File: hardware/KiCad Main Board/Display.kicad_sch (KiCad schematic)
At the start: 22 parts, among them J3 Display_Connector-0.5mmZIF-AE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, J5 RAKA, Q1 AO3400A

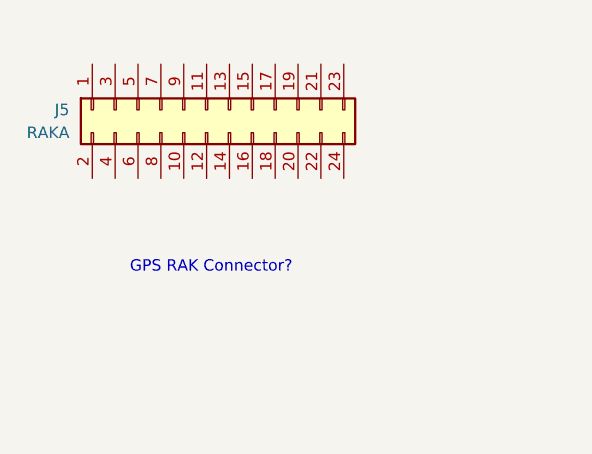
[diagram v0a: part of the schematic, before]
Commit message: added connector for RF daughter board
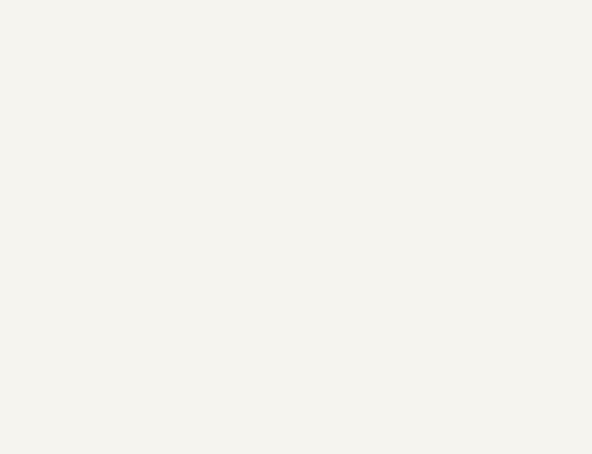
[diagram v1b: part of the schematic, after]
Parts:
- removed J5: RAKA, symbol Connector_Generic:Conn_02x12_Odd_Even
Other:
- note removed: "GPS RAK Connector?"
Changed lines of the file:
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@@
 	(generator_version "9.0")
 	(paper "A4")
-	(text "GPS RAK Connector?\n"
-		(exclude_from_sim no)
-		(at 75.438 64.516 0)
-		(effects
-			(font
-				(size 1.27 1.27)
-			)
-		)
-	)
 	(text "Display\n"
 		(exclude_from_sim no)
@@
 					(unit 1)
 				)
-			)
-		)
-	)
-	(symbol
-		(lib_id "Connector_Generic:Conn_02x12_Odd_Even")
-		(at 74.93 46.99 90)
-		(mirror x)
-		(unit 1)
-		(exclude_from_sim no)
-		(in_bom yes)
-		(on_board yes)
-		(dnp no)
-		(fields_autoplaced yes)
-		(property "Reference" "J5"
-			(at 59.69 46.9899 90)
-			(effects
-				(font
-					(size 1.27 1.27)
-				)
-				(justify left)
-			)
-		)
-		(property "Value" "RAKA"
-			(at 59.69 49.5299 90)
-			(effects
-				(font
-					(size 1.27 1.27)
-				)
-				(justify left)
-			)
-		)
-		(property "Footprint" ""
-			(at 74.93 46.99 0)
-			(effects
-				(font
-					(size 1.27 1.27)
-				)
-				(hide yes)
-			)
-		)
-		(property "Datasheet" "~"
-			(at 74.93 46.99 0)
-			(effects
-				(font
-					(size 1.27 1.27)
-				)
-				(hide yes)
-			)
-		)
-		(property "Description" "Generic connector, double row, 02x12, odd/even pin numbering scheme (row 1 odd numbers, row 2 even numbers), script generated (kicad-library-utils/schlib/autogen/connector/)"
-			(at 74.93 46.99 0)
-			(effects
-				(font
-					(size 1.27 1.27)
-				)
-				(hide yes)
-			)
-		)
-		(pin "19"
-		)
-		(pin "11"
-		)
-		(pin "7"
-		)
-		(pin "23"
-		)
-		(pin "12"
-		)
-		(pin "16"
-		)
-		(pin "5"
-		)
-		(pin "21"
-		)
-		(pin "6"
-		)
-		(pin "2"
-		)
-		(pin "15"
-		)
-		(pin "9"
-		)
-		(pin "1"
-		)
-		(pin "3"
-		)
-		(pin "13"
-		)
-		(pin "17"
-		)
-		(pin "4"
-		)
-		(pin "8"
-		)
-		(pin "10"
-		)
-		(pin "14"
-		)
-		(pin "18"
-		)
-		(pin "20"
-		)
-		(pin "22"
-		)
-		(pin "24"
-		)
-		(instances
-			(project ""
-				(path "/fd5c68a7-f5d0-4135-a258-bde3ebf63307/b6409364-80a7-45e6-8438-6c9767ff2100"
-					(reference "J5")
-					(unit 1)
-				)

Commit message: working on PCB
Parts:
- removed D1, D2, D3: MBR0530, Diode_SMD:D_SOD-123, symbol Diode:MBR0530
- added D56, D57, D58: B340, Diode_SMD:D_SMC, symbol Diode:B340
- J3: value Display_Connector-0.5mmZIF-AES200200A00-1.54ENRS -> FH12-24S-0.5SH(55); footprint (none) -> Connector_FFC-FPC:Hirose_FH12-24S-0.5SH_1x24-1MP_P0.50mm_Horizontal
- L2: footprint (none) -> Inductor_SMD:L_10.4x10.4_H4.8
- R13: footprint (none) -> Resistor_SMD:R_0805_2012Metric_Pad1.20x1.40mm_HandSolder
- R14, R15, R16: footprint (none) -> Resistor_SMD:R_0603_1608Metric_Pad0.98x0.95mm_HandSolder
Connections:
- net GND: now also D57.1 (K)
- net at C28.2, J3.21 (Pin_21): now also D58.1 (K)
- net at C26.1: now also D56.1 (K), D57.2 (A)
- net at C27.2, J3.23 (Pin_23): now also D56.2 (A)
- net at C26.2, L2.1, Q1.3 (D): now also D58.2 (A)
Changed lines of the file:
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@@
 			)
 		)
-		(property "Footprint" ""
+		(property "Footprint" "Resistor_SMD:R_0603_1608Metric_Pad0.98x0.95mm_HandSolder"
 			(at 204.47 114.3 0)
 			(effects
@@
 	)
 	(symbol
+		(lib_id "Diode:B340")
+		(at 195.58 59.69 0)
+		(unit 1)
+		(exclude_from_sim no)
+		(in_bom yes)
+		(on_board yes)
+		(dnp no)
+		(fields_autoplaced yes)
+		(property "Reference" "D58"
+			(at 195.2625 53.34 0)
+			(effects
+				(font
+					(size 1.27 1.27)
+				)
+			)
+		)
+		(property "Value" "B340"
+			(at 195.2625 55.88 0)
+			(effects
+				(font
+					(size 1.27 1.27)
+				)
+			)
+		)
+		(property "Footprint" "Diode_SMD:D_SMC"
+			(at 195.58 64.135 0)
+			(effects
+				(font
+					(size 1.27 1.27)
+				)
+				(hide yes)
+			)
+		)
+		(property "Datasheet" "http://www.jameco.com/Jameco/Products/ProdDS/1538777.pdf"
+			(at 195.58 59.69 0)
+			(effects
+				(font
+					(size 1.27 1.27)
+				)
+				(hide yes)
+			)
+		)
+		(property "Description" "40V 3A Schottky Barrier Rectifier Diode, SMC"
+			(at 195.58 59.69 0)
+			(effects
+				(font
+					(size 1.27 1.27)
+				)
+				(hide yes)
+			)
+		)
+		(pin "1"
+		)
+		(pin "2"
+		)
+		(instances
+			(project "OSS Radio Hardware Design"
+				(path "/fd5c68a7-f5d0-4135-a258-bde3ebf63307/b6409364-80a7-45e6-8438-6c9767ff2100"
+					(reference "D58")
+					(unit 1)
+				)
+			)
+		)
+	)
+	(symbol
 		(lib_id "Device:R_Small")
 		(at 212.09 99.06 270)
@@
 			)
 		)
-		(property "Footprint" ""
+		(property "Footprint" "Resistor_SMD:R_0603_1608Metric_Pad0.98x0.95mm_HandSolder"
 			(at 212.09 99.06 0)
 			(effects
@@
 	)
 	(symbol
-		(lib_id "Diode:MBR0530")
-		(at 213.36 46.99 180)
-		(unit 1)
-		(exclude_from_sim no)
-		(in_bom yes)
-		(on_board yes)
-		(dnp no)
-		(fields_autoplaced yes)
-		(property "Reference" "D3"
-			(at 213.6775 40.64 0)
-			(effects
-				(font
-					(size 1.27 1.27)
-				)
-			)
-		)
-		(property "Value" "MBR0530"
-			(at 213.6775 43.18 0)
-			(effects
-				(font
-					(size 1.27 1.27)
-				)
-			)
-		)
-		(property "Footprint" "Diode_SMD:D_SOD-123"
-			(at 213.36 42.545 0)
-			(effects
-				(font
-					(size 1.27 1.27)
-				)
-				(hide yes)
-			)
-		)
-		(property "Datasheet" "http://www.mccsemi.com/up_pdf/MBR0520~MBR0580(SOD123).pdf"
-			(at 213.36 46.99 0)
-			(effects
-				(font
-					(size 1.27 1.27)
-				)
-				(hide yes)
-			)
-		)
-		(property "Description" "30V 0.5A Schottky Power Rectifier Diode, SOD-123"
-			(at 213.36 46.99 0)
-			(effects
-				(font
-					(size 1.27 1.27)
-				)
-				(hide yes)
-			)
-		)
-		(pin "1"
-		)
-		(pin "2"
-		)
-		(instances
-			(project "OSS Radio Hardware Design"
-				(path "/fd5c68a7-f5d0-4135-a258-bde3ebf63307/b6409364-80a7-45e6-8438-6c9767ff2100"
-					(reference "D3")
-					(unit 1)
-				)
-			)
-		)
-	)
-	(symbol
 		(lib_id "power:GND")
 		(at 166.37 38.1 270)
@@
 			)
 		)
-		(property "Footprint" ""
+		(property "Footprint" "Resistor_SMD:R_0603_1608Metric_Pad0.98x0.95mm_HandSolder"
 			(at 214.63 91.44 0)
 			(effects
@@
 	)
 	(symbol
+		(lib_id "Diode:B340")
+		(at 213.36 46.99 180)
+		(unit 1)
+		(exclude_from_sim no)
+		(in_bom yes)
+		(on_board yes)
+		(dnp no)
+		(fields_autoplaced yes)
+		(property "Reference" "D57"
+			(at 213.6775 40.64 0)
+			(effects
+				(font
+					(size 1.27 1.27)
+				)
+			)
+		)
+		(property "Value" "B340"
+			(at 213.6775 43.18 0)
+			(effects
+				(font
+					(size 1.27 1.27)
+				)
+			)
+		)
+		(property "Footprint" "Diode_SMD:D_SMC"
+			(at 213.36 42.545 0)
+			(effects
+				(font
+					(size 1.27 1.27)
+				)
+				(hide yes)
+			)
+		)
+		(property "Datasheet" "http://www.jameco.com/Jameco/Products/ProdDS/1538777.pdf"
+			(at 213.36 46.99 0)
+			(effects
+				(font
+					(size 1.27 1.27)
+				)
+				(hide yes)
+			)
+		)
+		(property "Description" "40V 3A Schottky Barrier Rectifier Diode, SMC"
+			(at 213.36 46.99 0)
+			(effects
+				(font
+					(size 1.27 1.27)
+				)
+				(hide yes)
+			)
+		)
+		(pin "1"
+		)
+		(pin "2"
+		)
+		(instances
+			(project "OSS Radio Hardware Design"
+				(path "/fd5c68a7-f5d0-4135-a258-bde3ebf63307/b6409364-80a7-45e6-8438-6c9767ff2100"
+					(reference "D57")
+					(unit 1)
+				)
+			)
+		)
+	)
+	(symbol
 		(lib_id "Device:R_Small")
 		(at 196.85 78.74 90)
@@
 			)
 		)
-		(property "Footprint" ""
+		(property "Footprint" "Resistor_SMD:R_0805_2012Metric_Pad1.20x1.40mm_HandSolder"
 			(at 196.85 78.74 0)
 			(effects
@@
 	)
 	(symbol
+		(lib_id "Diode:B340")
+		(at 195.58 46.99 180)
+		(unit 1)
+		(exclude_from_sim no)
+		(in_bom yes)
+		(on_board yes)
+		(dnp no)
+		(fields_autoplaced yes)
+		(property "Reference" "D56"
+			(at 195.8975 40.64 0)
+			(effects
+				(font
+					(size 1.27 1.27)
+				)
+			)
+		)
+		(property "Value" "B340"
+			(at 195.8975 43.18 0)
+			(effects
+				(font
+					(size 1.27 1.27)
+				)
+			)
+		)
+		(property "Footprint" "Diode_SMD:D_SMC"
+			(at 195.58 42.545 0)
+			(effects
+				(font
+					(size 1.27 1.27)
+				)
+				(hide yes)
+			)
+		)
+		(property "Datasheet" "http://www.jameco.com/Jameco/Products/ProdDS/1538777.pdf"
+			(at 195.58 46.99 0)
+			(effects
+				(font
+					(size 1.27 1.27)
+				)
+				(hide yes)
+			)
+		)
+		(property "Description" "40V 3A Schottky Barrier Rectifier Diode, SMC"
+			(at 195.58 46.99 0)
+			(effects
+				(font
+					(size 1.27 1.27)
+				)
+				(hide yes)
+			)
+		)
+		(pin "1"
+		)
+		(pin "2"
+		)
+		(instances
+			(project "OSS Radio Hardware Design"
+				(path "/fd5c68a7-f5d0-4135-a258-bde3ebf63307/b6409364-80a7-45e6-8438-6c9767ff2100"
+					(reference "D56")
+					(unit 1)
+				)
+			)
+		)
+	)
+	(symbol
 		(lib_id "Device:C_Small")
 		(at 223.52 83.82 90)
@@
 			)
 		)
-		(property "Footprint" ""
+		(property "Footprint" "Inductor_SMD:L_10.4x10.4_H4.8"
 			(at 219.71 59.69 0)
 			(effects
@@
 			)
 		)
-		(property "Datasheet" "~"
+		(property "Datasheet" "SMDRH104R-470MT"
 			(at 219.71 59.69 0)
 			(effects
@@
 			)
 		)
-		(property "Value" "Display_Connector-0.5mmZIF-AES200200A00-1.54ENRS"
+		(property "Value" "FH12-24S-0.5SH(55)"
 			(at 244.348 77.47 90)
 			(effects
@@
 			)
 		)
-		(property "Footprint" ""
+		(property "Footprint" "Connector_FFC-FPC:Hirose_FH12-24S-0.5SH_1x24-1MP_P0.50mm_Horizontal"
 			(at 238.76 101.6 0)
 			(effects
@@
 				(path "/fd5c68a7-f5d0-4135-a258-bde3ebf63307/b6409364-80a7-45e6-8438-6c9767ff2100"
 					(reference "J3")
-					(unit 1)
-				)
-			)
-		)
-	)
-	(symbol
-		(lib_id "Diode:MBR0530")
-		(at 195.58 46.99 180)
-		(unit 1)
-		(exclude_from_sim no)
-		(in_bom yes)
-		(on_board yes)
-		(dnp no)
-		(fields_autoplaced yes)
-		(property "Reference" "D2"
-			(at 195.8975 40.64 0)
-			(effects
-				(font
-					(size 1.27 1.27)
-				)
-			)
-		)
-		(property "Value" "MBR0530"
-			(at 195.8975 43.18 0)
-			(effects
-				(font
-					(size 1.27 1.27)
-				)
-			)
-		)
-		(property "Footprint" "Diode_SMD:D_SOD-123"
-			(at 195.58 42.545 0)
-			(effects
-				(font
-					(size 1.27 1.27)
-				)
-				(hide yes)
-			)
-		)
-		(property "Datasheet" "http://www.mccsemi.com/up_pdf/MBR0520~MBR0580(SOD123).pdf"
-			(at 195.58 46.99 0)
-			(effects
-				(font
-					(size 1.27 1.27)
-				)
-				(hide yes)
-			)
-		)
-		(property "Description" "30V 0.5A Schottky Power Rectifier Diode, SOD-123"
-			(at 195.58 46.99 0)
-			(effects
-				(font
-					(size 1.27 1.27)
-				)
-				(hide yes)
-			)
-		)
-		(pin "1"
-		)
-		(pin "2"
-		)
-		(instances
-			(project "OSS Radio Hardware Design"
-				(path "/fd5c68a7-f5d0-4135-a258-bde3ebf63307/b6409364-80a7-45e6-8438-6c9767ff2100"
-					(reference "D2")
 					(unit 1)
 				)
@@
 					(unit 1)
 				)
-			)
-		)
-	)
-	(symbol
-		(lib_id "Diode:MBR0530")
-		(at 195.58 59.69 0)
-		(unit 1)
-		(exclude_from_sim no)
-		(in_bom yes)
-		(on_board yes)
-		(dnp no)
-		(fields_autoplaced yes)
-		(property "Reference" "D1"
-			(at 195.2625 53.34 0)
-			(effects
-				(font
-					(size 1.27 1.27)
-				)
-			)
-		)
-		(property "Value" "MBR0530"
-			(at 195.2625 55.88 0)
-			(effects
-				(font
-					(size 1.27 1.27)
-				)
-			)
-		)
-		(property "Footprint" "Diode_SMD:D_SOD-123"
-			(at 195.58 64.135 0)
-			(effects
-				(font
-					(size 1.27 1.27)
-				)
-				(hide yes)
-			)
-		)
-		(property "Datasheet" "http://www.mccsemi.com/up_pdf/MBR0520~MBR0580(SOD123).pdf"
-			(at 195.58 59.69 0)
-			(effects
-				(font
-					(size 1.27 1.27)
-				)
-				(hide yes)
-			)
-		)
-		(property "Description" "30V 0.5A Schottky Power Rectifier Diode, SOD-123"
-			(at 195.58 59.69 0)
-			(effects
-				(font
-					(size 1.27 1.27)
-				)
-				(hide yes)
-			)
-		)
-		(pin "1"
-		)
-		(pin "2"
-		)
-		(instances
-			(project ""
-				(path "/fd5c68a7-f5d0-4135-a258-bde3ebf63307/b6409364-80a7-45e6-8438-6c9767ff2100"
-					(reference "D1")
-					(unit 1)
-				)

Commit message: mostly designed PCB
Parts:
- D56, D57, D58: footprint Diode_SMD:D_SMC -> Diode_SMD:D_SMA
- L2: footprint Inductor_SMD:L_10.4x10.4_H4.8 -> CDRH2D18_LDNP-470NC:CDRH2D18_LDNP-470NC
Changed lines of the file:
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@@
 			)
 		)
-		(property "Footprint" "Diode_SMD:D_SMC"
+		(property "Footprint" "Diode_SMD:D_SMA"
 			(at 195.58 64.135 0)
 			(effects
@@
 			)
 		)
-		(property "Footprint" "Diode_SMD:D_SMC"
+		(property "Footprint" "Diode_SMD:D_SMA"
 			(at 213.36 42.545 0)
 			(effects
@@
 			)
 		)
-		(property "Footprint" "Diode_SMD:D_SMC"
+		(property "Footprint" "Diode_SMD:D_SMA"
 			(at 195.58 42.545 0)
 			(effects
@@
 			)
 		)
-		(property "Footprint" "Inductor_SMD:L_10.4x10.4_H4.8"
+		(property "Footprint" "CDRH2D18_LDNP-470NC:CDRH2D18_LDNP-470NC"
 			(at 219.71 59.69 0)
 			(effects
@@
 			)
 		)
-		(property "Datasheet" "SMDRH104R-470MT"
+		(property "Datasheet" "CDRH2D18_LDNP-470NC"
 			(at 219.71 59.69 0)
 			(effects
